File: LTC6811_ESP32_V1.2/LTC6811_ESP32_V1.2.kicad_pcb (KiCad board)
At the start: 2 copper layers, 130 x 90 mm, 255 parts, among them J1 +12V, J10 Hole /NC, J11 Hole /NC, J12 Hole /NC, J13 B7B-XH-A, J14 B7B-XH-A, J15 PB MB, J2 OLED /NC, J3 CAN /NC, J4 USB, J5 UART /NC, J6 JTAG /NC, J7 Boot Option /NC, J8 SERIAL /NC, J9 GND, Q1 BSS138, Q10 TSM2323, Q11 TSM2323, Q12 TSM2323, Q13 TSM2323, Q14 TSM2323, Q2 NSV1C201MZ4, Q3 TSM2323, Q4 TSM2323, Q5 TSM2323, Q6 TSM2323, Q7 TSM2323, Q8 TSM2323, Q9 TSM2323, U1 TPS76350, U10 CP2104, U11 ISO1050DUBR, U12 LTC6811HG-1, U2 AMC1301 or AMC1302, U3 AMC1301, U4 SN6501DBV, U5 OPA2197IDR, U6 ISL28022, U7 TPS563231, U8 ESP32-DevKitC V4, U9 LTC6820

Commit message: Add files via upload
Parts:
- C39: value 2.2uF 16V -> 4.7uF 16V
- J1: value +12V -> PB MB; footprint Connector_PinHeader_2.54mm:PinHeader_1x01_P2.54mm_Vertical -> Connector_JST:JST_VH_B2P-VH-B_1x02_P3.96mm_Vertical
- J6: moved to F.Cu
- J8: footprint Connector_PinHeader_2.54mm:PinHeader_1x05_P2.54mm_Vertical -> Connector_PinHeader_2.54mm:PinHeader_1x04_P2.54mm_Vertical; moved to F.Cu
- J9: value GND -> Hole /NC; footprint Connector_PinHeader_2.54mm:PinHeader_1x01_P2.54mm_Vertical -> MountingHole:MountingHole_3.2mm_M3_ISO7380_Pad
- R17: footprint Resistor_SMD:R_2010_5025Metric -> Resistor_SMD:R_0603_1608Metric
- TR1: value TRANSF5 -> Converters
- moved C11 161.0 mm to (108.0, 111.5)
- moved C8 161.0 mm to (109.7, 111.6)
- moved R17 156.3 mm to (114.2, 114.6), turned to 0 degrees
- moved U2 153.5 mm to (117.3, 110.5), turned to 180 degrees
- moved C4 150.7 mm to (117.3, 114.6), turned to 180 degrees
- moved U5 149.5 mm to (112.2, 96.1), turned to 180 degrees
- moved R16 146.7 mm to (120.4, 114.6), turned to 180 degrees
- moved C5 143.4 mm to (126.0, 112.4), turned to 0 degrees
- moved J9 139.4 mm to (188.1, 55.5)
- moved R30 130.4 mm to (121.0, 68.2)
- moved R32 130.4 mm to (121.0, 66.7)
- moved C14 130.4 mm to (118.1, 72.8)
- moved C16 130.4 mm to (118.0, 68.1)
- moved C19 130.4 mm to (123.3, 67.4)
- moved C20 130.4 mm to (118.0, 65.1)
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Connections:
- net /PowerMonitor/Vbat renamed /PowerMonitor/VBAT_SENSE
- BAT-1 pad 1: GND -> /PowerMonitor/BAT-
- C1 pad 1: /PowerSupply/ISO+5V -> /PowerMonitor/ISO+5V
- J2 pad 2: /MCU/OLED_SDA -> /MCU/OLED_RST
- J2 pad 3: /MCU/OLED_RST -> /MCU/OLED_SDA
- J3 pad 1: /CAN/5V_CAN -> /CAN/CAN_GND
- J3 pad 4: /CAN/CAN_GND -> /CAN/5V_CAN
- J8 pad 4: unconnected-(J8-Pin_4-Pad4) -> +3V3
- J9 pad 1: GND -> unconnected-(J9-Pin_1-Pad1)
- L1 pad 1: Net-(U7-BST) -> Net-(U7-SW)
- R10 pad 2: /PowerSupply/ISO+5V -> /PowerMonitor/ISO+5V
- R13 pad 2: GND -> /PowerMonitor/BAT-
- R17 pad 1: GND -> /PowerMonitor/BAT-
- R6 pad 1: /MCU/OLED_SDA -> /MCU/OLED_RST
- R7 pad 2: /MCU/OLED_RST -> /MCU/OLED_SDA
- TR1 pad 1: Net-(U4-D1) -> Net-(U4-D2)
- TR1 pad 3: Net-(U4-D2) -> Net-(U4-D1)
- TR1 pad 4: Net-(D5-A) -> Net-(D4-A)
- TR1 pad 6: Net-(D4-A) -> Net-(D5-A)
- U1 pad 5: /PowerSupply/ISO+5V -> /PowerMonitor/ISO+5V
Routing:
- net /LTC6811/C6: track 18.4 -> 0.00 mm
- net /BAT+: track 43.1 -> 31.8 mm
- net /LTC6811/C1_G: track 9.51 -> 0.00 mm
- net /LTC6811/cell3/C: track 25.8 -> 16.8 mm
- net GND_PACK: track 49.3 -> 41.0 mm, vias 105 -> 2
- net /LTC6811/cell2/C: track 27.5 -> 19.5 mm
- net /LTC6811/cell10/S: track 19.2 -> 27.2 mm
- net /LTC6811/cell11/S: track 23.0 -> 30.9 mm
- net /LTC6811/cell4/C: track 21.9 -> 14.1 mm
- net /LTC6811/C11: track 7.71 -> 0.00 mm
- net /LTC6811/C1: track 7.46 -> 0.00 mm
- net /LTC6811/cell12/S: track 25.4 -> 32.9 mm
- net /LTC6811/cell12/C: track 25.4 -> 32.8 mm
- net /LTC6811/cell9/S: track 15.6 -> 22.7 mm
- net /LTC6811/cell8/C: track 15.5 -> 22.4 mm
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- removed copper zone on B.Cu, net GND
- removed copper zone on F.Cu, net GND
- removed copper zone on B.Cu, net GND_PACK
- removed copper zone on F.Cu, net GND_PACK
- removed copper zone on F.Cu, net Net-(U7-BST)
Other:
- board text added: "+12V"
- board text removed: "12/24V"

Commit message: Add files via upload
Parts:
- removed C25: 47uF/10V, Capacitor_SMD:C_1206_3216Metric
- removed R41: 45.3K, Resistor_SMD:R_0603_1608Metric
- removed R42: 10K, Resistor_SMD:R_0603_1608Metric
- added C10: 10uF/16V, Capacitor_SMD:C_0805_2012Metric, F.Cu at (78.6, 117.5)
- added C3: 2.2uF 50V, Capacitor_SMD:C_0603_1608Metric, F.Cu at (85.8, 126.5)
- added R37: 100K, Resistor_SMD:R_0603_1608Metric, F.Cu at (92.3, 121.8)
- added R38: 22.1K, Resistor_SMD:R_0603_1608Metric, F.Cu at (90.7, 121.8)
- C24: value 10uF 25V -> 10uF/16V
- J2: moved to B.Cu
- U7: value TPS563231 -> LM51420; footprint Package_TO_SOT_SMD:SOT-563 -> Package_TO_SOT_SMD:SOT-23-6_Handsoldering
- moved R35 59.2 mm to (99.2, 112.1), turned to 90 degrees
- moved R36 56.8 mm to (100.8, 112.1), turned to 90 degrees
- moved R10 54.9 mm to (129.5, 93.5), turned to 0 degrees
- moved D3 54.8 mm to (128.7, 95.9), turned to 90 degrees
- moved C21 54.0 mm to (104.4, 112.1), turned to 180 degrees
- moved U6 50.8 mm to (101.4, 108.5), turned to 0 degrees
- moved C18 49.6 mm to (105.9, 109.8), turned to 90 degrees
- moved C20 45.9 mm to (107.5, 109.8), turned to 90 degrees
- moved R31 45.8 mm to (109.1, 111.5), turned to -90 degrees
- moved C16 44.0 mm to (110.7, 111.5), turned to -90 degrees
- moved R32 43.4 mm to (109.1, 108.4), turned to -90 degrees
- moved C19 42.4 mm to (107.5, 106.7), turned to -90 degrees
- moved R25 42.1 mm to (113.1, 112.3), turned to 180 degrees
- moved R30 41.5 mm to (110.7, 108.4), turned to -90 degrees
- moved R24 39.9 mm to (112.3, 109.8), turned to -90 degrees
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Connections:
- C24 pad 1: /PowerSupply/+12V -> +3V3
- C28 pad 2: Net-(U7-BST) -> Net-(U7-CB)
- J1 pad 1: /PowerSupply/+12V -> +12V
- J6 pad 3: /MCU/MTCK -> /MCU/MTDO
- J6 pad 4: /MCU/MTDO -> /MCU/MTCK
- U7 pad 1: /PowerSupply/+12V -> GND
- U7 pad 3: GND -> +12V
- U7 pad 4: Net-(U7-BST) -> Net-(U7-FB)
- U7 pad 5: /PowerSupply/+12V -> +12V
- U7 pad 6: Net-(U7-FB) -> Net-(U7-CB)
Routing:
- net +3V3: track 0.00 -> 248.8 mm
- net /MCU/SCL: track 0.00 -> 49.9 mm
- net /MCU/SDA: track 0.00 -> 42.7 mm
- net /PowerMonitor/ISO+5V: track 0.00 -> 35.1 mm, vias 0 -> 2
- net Net-(J15-Pin_2): track 0.00 -> 32.4 mm
- net Net-(J15-Pin_1): track 0.00 -> 32.4 mm
- net Net-(R14-Pad2): track 0.00 -> 27.8 mm
- net Net-(U9-IM): track 0.00 -> 24.1 mm, vias 0 -> 2
- net Net-(U9-IP): track 0.00 -> 24.0 mm, vias 0 -> 2
- net /MCU/MOSI: track 0.00 -> 21.0 mm
- net /LTC6811/C6: track 0.00 -> 20.9 mm
- net /BAT+: track 31.8 -> 52.4 mm
- net +12V: track 0.00 -> 20.1 mm, vias 0 -> 2
- net GND: track 0.00 -> 19.6 mm
- net Net-(C49-Pad1): track 27.1 -> 45.7 mm, vias 2 -> 0
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- added copper zone on B.Cu, net /CAN/CAN_GND
- added copper zone on F.Cu, net /CAN/CAN_GND
- added copper zone on B.Cu, net /PowerMonitor/BAT-
- added copper zone on F.Cu, net /PowerMonitor/BAT-
- added copper zone on B.Cu, net GND
- added copper zone on F.Cu, net GND
- added copper zone on B.Cu, net GND_PACK
- added copper zone on F.Cu, net GND_PACK
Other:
- board text added: "PACK-"

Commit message: Add files via upload
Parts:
- BZ1: footprint ENNOID:BUZZER -> Buzzer_Beeper:Beeper_AI-1027-TWT-5V
- moved LOGO1 87.7 mm to (154.2, 117.1)
- moved J1 19.5 mm to (67.4, 127.1), turned to 90 degrees
- moved J3 15.6 mm to (114.2, 52.7), turned to 90 degrees
- moved C36 9.04 mm to (105.0, 85.4)
- moved J5 7.60 mm to (104.3, 71.6), turned to 180 degrees
- moved C37 5.98 mm to (105.0, 83.8)
- moved C44 5.63 mm to (121.8, 57.0)
- moved U11 4.82 mm to (113.1, 60.3)
- moved C45 4.24 mm to (120.2, 57.0)
- moved C43 4.00 mm to (105.6, 57.3), turned to -90 degrees
- moved D8 3.41 mm to (121.2, 60.3)
- moved C23 3.08 mm to (102.8, 96.8), turned to 90 degrees
- moved D1 2.97 mm to (95.8, 113.8), turned to 90 degrees
- moved C71 1.88 mm to (104.4, 96.8), turned to -90 degrees
- moved C42 1.81 mm to (104.0, 57.3), turned to -90 degrees
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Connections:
- J5 pad 2: /MCU/CAN_TX -> /MCU/CAN_RX
- J5 pad 3: /MCU/CAN_RX -> /MCU/CAN_TX
- J8 pad 1: GND -> +3V3
- J8 pad 4: +3V3 -> GND
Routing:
- net +12V: track 20.1 -> 75.7 mm, vias 2 -> 4
- net +3V3: track 248.8 -> 300.7 mm, vias 0 -> 3
- net /MCU/MTDO: track 0.00 -> 32.5 mm, vias 0 -> 1
- net GND_PACK: track 41.4 -> 57.9 mm
- net /CAN/CAN_GND: track 0.00 -> 7.28 mm
- net Net-(U9-IM): track 24.1 -> 28.8 mm
- net /MCU/OLED_SCL: track 4.20 -> 8.86 mm
- net GND: track 19.6 -> 24.3 mm
- net /CAN/CAN_RX: track 16.8 -> 12.2 mm
- net /CAN/CAN_TX: track 11.0 -> 6.71 mm
- net /MCU/TX_USB: track 2.92 -> 6.77 mm
- net /MCU/RX_USB: track 2.87 -> 6.58 mm
- net /PowerMonitor/VBAT_SENSE: track 17.0 -> 19.4 mm
- net Net-(U5B--): track 6.45 -> 8.48 mm
- net /LTC6811/cell11/C+: track 13.5 -> 15.4 mm
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- added copper zone on F.Cu, net +3V3
- removed copper zone on F.Cu, net Net-(C49-Pad1)
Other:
- board text removed: "+"
- board text removed: "-"
- board text removed: "B-"

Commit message: finished
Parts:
- added TP1: TestPoint, TestPoint:TestPoint_Pad_D1.0mm, F.Cu at (130.5, 95.3)
- added TP2: TestPoint, TestPoint:TestPoint_Pad_D1.0mm, F.Cu at (95.1, 113.1)
- added TP3: TestPoint, TestPoint:TestPoint_Pad_D1.0mm, F.Cu at (143.5, 85.6)
- added TP4: TestPoint, TestPoint:TestPoint_Pad_D1.0mm, F.Cu at (158.9, 73.3)
- moved R8 15.1 mm to (90.8, 107.5), turned to -90 degrees
- moved R6 11.6 mm to (92.4, 107.5), turned to -90 degrees
- moved R37 11.4 mm to (82.9, 128.4), turned to 180 degrees
- moved C36 9.68 mm to (113.9, 81.6), turned to 90 degrees
- moved C10 9.39 mm to (87.4, 114.2), turned to -90 degrees
- moved R38 9.20 mm to (82.9, 126.8), turned to 0 degrees
- moved C3 8.78 mm to (78.3, 121.3), turned to -90 degrees
- moved C24 8.54 mm to (85.3, 114.2), turned to -90 degrees
- moved L1 8.31 mm to (81.1, 115.5), turned to 90 degrees
- moved C37 7.62 mm to (112.3, 81.6), turned to -90 degrees
- moved C28 7.01 mm to (82.9, 125.2), turned to 180 degrees
- moved R1 6.00 mm to (91.3, 114.3), turned to 90 degrees
- moved D1 5.83 mm to (91.3, 117.5)
- moved U7 4.96 mm to (81.1, 121.9), turned to -90 degrees
- moved D11 4.33 mm to (172.0, 118.3)
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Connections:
- J1 pad 1: +12V -> GND
- J1 pad 2: GND -> +12V
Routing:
- net GND: track 24.3 -> 85.3 mm, vias 0 -> 164
- net +3V3: track 300.7 -> 255.6 mm, vias 3 -> 2
- net GND_PACK: track 57.9 -> 100.7 mm, vias 2 -> 181
- net /BAT+: track 52.4 -> 43.3 mm
- net +12V: track 75.7 -> 67.7 mm, vias 4 -> 6
- net /MCU/OLED_SCL: track 8.86 -> 14.1 mm
- net /LTC6811/Vref2: track 25.7 -> 29.9 mm, vias 3 -> 4
- net /LTC6811/cell7/C: track 22.1 -> 18.0 mm
- net Net-(C49-Pad1): track 45.7 -> 49.2 mm
- net /LTC6811/T5: track 25.0 -> 22.6 mm
- net /LTC6811/cell4/C+: track 17.3 -> 15.5 mm
- net /LTC6811/cell1/C+: track 17.1 -> 15.4 mm
- net /LTC6811/Vreg: track 21.8 -> 20.2 mm, vias 2 -> 0
- net /LTC6811/cell8/C+: track 14.6 -> 16.3 mm
- net /LTC6811/T2: track 23.4 -> 24.9 mm
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- added copper zone on F.Cu, net Net-(C49-Pad1)
- added copper zone on F.Cu, net Net-(U7-SW)
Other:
- board text added: "3.3V"
- board text added: "MB PB"
- board text added: "Vreg"
- board text removed: "3V3"

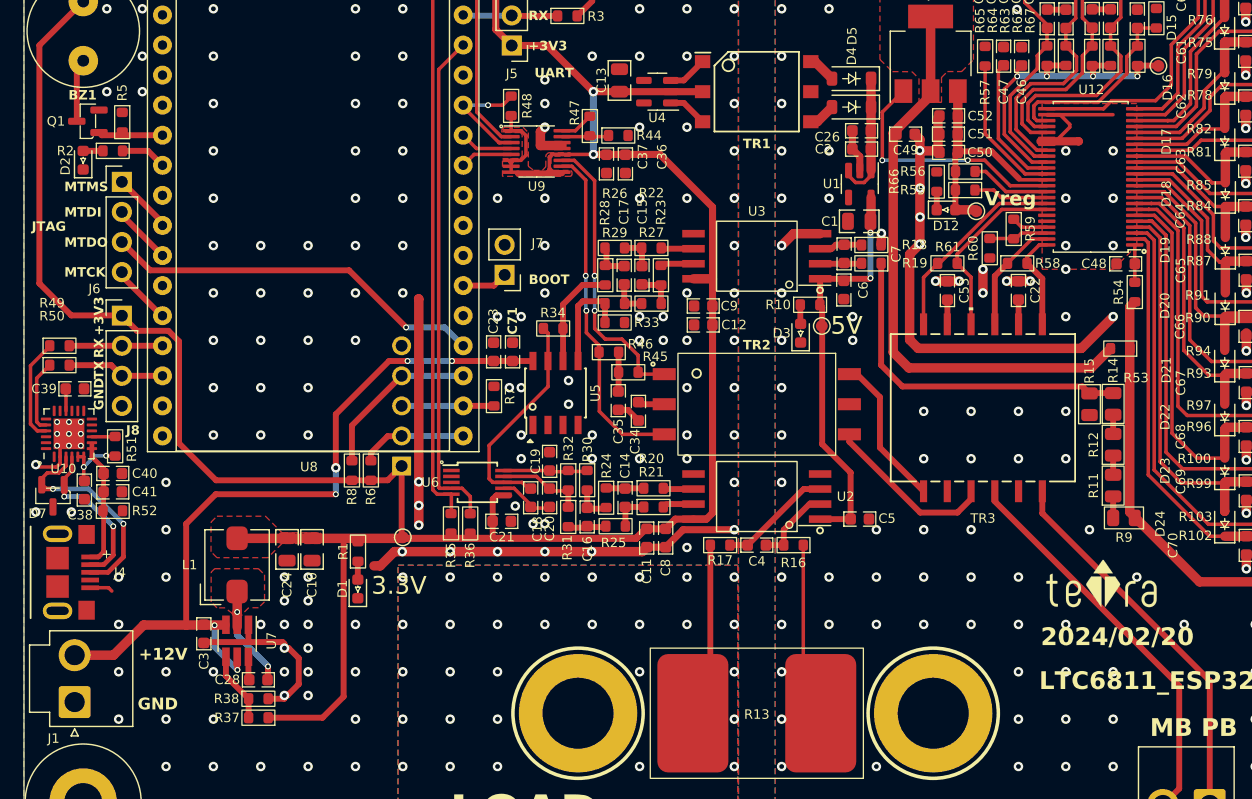
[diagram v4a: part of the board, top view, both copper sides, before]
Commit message: add BOM
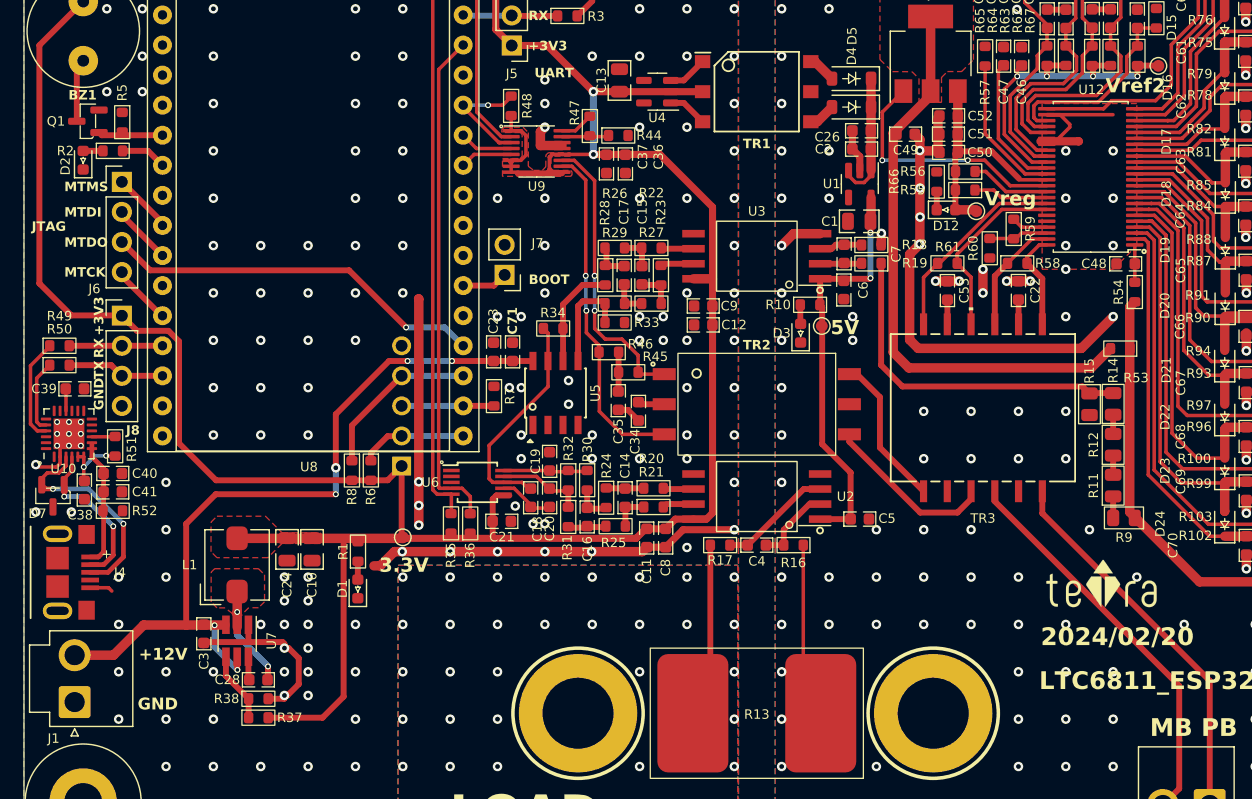
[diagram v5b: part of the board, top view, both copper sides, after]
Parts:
- C1, C13: value 10uF 25V -> 10uF/16V
- C11, C12, C38, C41: value 2.2uF 16V -> 2.2uF/25V
- C14, C15: value 2.2nF 16V -> 2.2nF/16V
- C16, C17: value 220pF 50V -> 220pF/50V
- C18, C19, C2, C20, C21, C23, C28, C37, C40, C43, C48, C49, C5, C54, C55, C56, C57, C58, C59, C6, C60, C61, C62, C63, C64, C65, C66, C67, C68, C69, C70, C8, C9: value 100nF 100V -> 100nF/100V
- C22, C53: value 100pF 100V -> 100pF/100V
- C3: value 2.2uF 50V -> 2.2uF/25V
- C32, C33, C45: value 100nF 50V -> 100nF/100V
- C34, C35: value 10nF 100V -> 10nF/100V
- C36, C42, C44, C46, C47, C50, C51, C52, C71: value 1uF 25V -> 1uF/25V
- C39: value 4.7uF 16V -> 4.7uF/16V
- C4, C7: value 330pF 100V -> 330pF/100V
- TR1: value Converters -> Transformer
- U7: value LM51420 -> LMR51420XDDCR
- turned R37 to 0 degrees
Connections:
- R37 pad 1: +3V3 -> Net-(U7-FB)
- R37 pad 2: Net-(U7-FB) -> +3V3
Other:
- board text added: "Vref2"

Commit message: Add files via upload
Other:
- board text removed: "B"
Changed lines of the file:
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@@
     (effects (font (size 0.8 0.8) (thickness 0.15) bold) (justify left bottom))
-  )
-  (gr_text "B" (at 251 153.1) (layer "F.SilkS")
-    (effects (font (size 2 2) (thickness 0.3)) (justify left bottom))
   )
   (gr_text "PACK-" (at 131.75 139.05) (layer "F.SilkS")
